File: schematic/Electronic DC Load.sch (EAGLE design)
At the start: 104 parts, among them J1 POWER_JACKPTH_LOCK, J2 AVR_SPI_PROG_3X2PTH, J3 FAN, J4 KF762-2, Q1 16MHz, Q2 IRFP250NV, Q3 600mA/40V, U1 AMS1117-5.0, U10 AD8629ARZ, U2 REF5050_D_8, U3 ATMEGA328P_TQFP, U4 MP1584EN, U5 LM35_LP_3, U6 AD7190BRUZ, U7 AD5541ARZ, U8 INA210AIDCKRG4, U9 PCF8574_DW_16

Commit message: Change debouncing filter network resistor to 1K
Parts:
- R12, R17, R19, R22, R24, R25, R27: value 10K -> 1K
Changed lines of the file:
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@@
 <part name="P+14" library="supply1" library_urn="urn:adsk.eagle:library:371" deviceset="+5V" device=""/>
 <part name="P+15" library="supply1" library_urn="urn:adsk.eagle:library:371" deviceset="+5V" device=""/>
-<part name="R22" library="resistor" library_urn="urn:adsk.eagle:library:348" deviceset="R-EU_" device="R0603" package3d_urn="urn:adsk.eagle:package:26057/1" value="10K"/>
-<part name="R24" library="resistor" library_urn="urn:adsk.eagle:library:348" deviceset="R-EU_" device="R0603" package3d_urn="urn:adsk.eagle:package:26057/1" value="10K"/>
+<part name="R22" library="resistor" library_urn="urn:adsk.eagle:library:348" deviceset="R-EU_" device="R0603" package3d_urn="urn:adsk.eagle:package:26057/1" value="1K"/>
+<part name="R24" library="resistor" library_urn="urn:adsk.eagle:library:348" deviceset="R-EU_" device="R0603" package3d_urn="urn:adsk.eagle:package:26057/1" value="1K"/>
 <part name="GND18" library="supply1" library_urn="urn:adsk.eagle:library:371" deviceset="GND" device=""/>
 <part name="R16" library="resistor" library_urn="urn:adsk.eagle:library:348" deviceset="R-EU_" device="R0603" package3d_urn="urn:adsk.eagle:package:26057/1" value="10K"/>
 <part name="C20" library="resistor" library_urn="urn:adsk.eagle:library:348" deviceset="C-EU" device="C0603" package3d_urn="urn:adsk.eagle:package:26138/1" value="100nF"/>
 <part name="P+8" library="supply1" library_urn="urn:adsk.eagle:library:371" deviceset="+5V" device=""/>
-<part name="R12" library="resistor" library_urn="urn:adsk.eagle:library:348" deviceset="R-EU_" device="R0603" package3d_urn="urn:adsk.eagle:package:26057/1" value="10K"/>
+<part name="R12" library="resistor" library_urn="urn:adsk.eagle:library:348" deviceset="R-EU_" device="R0603" package3d_urn="urn:adsk.eagle:package:26057/1" value="1K"/>
 <part name="C25" library="resistor" library_urn="urn:adsk.eagle:library:348" deviceset="C-EU" device="C0603" package3d_urn="urn:adsk.eagle:package:26138/1" value="100nF"/>
 <part name="C28" library="resistor" library_urn="urn:adsk.eagle:library:348" deviceset="C-EU" device="C0603" package3d_urn="urn:adsk.eagle:package:26138/1" value="100nF"/>
@@
 <part name="P+13" library="supply1" library_urn="urn:adsk.eagle:library:371" deviceset="+5V" device=""/>
 <part name="R20" library="resistor" library_urn="urn:adsk.eagle:library:348" deviceset="R-EU_" device="R0603" package3d_urn="urn:adsk.eagle:package:26057/1" value="10K"/>
-<part name="R19" library="resistor" library_urn="urn:adsk.eagle:library:348" deviceset="R-EU_" device="R0603" package3d_urn="urn:adsk.eagle:package:26057/1" value="10K"/>
+<part name="R19" library="resistor" library_urn="urn:adsk.eagle:library:348" deviceset="R-EU_" device="R0603" package3d_urn="urn:adsk.eagle:package:26057/1" value="1K"/>
 <part name="C24" library="resistor" library_urn="urn:adsk.eagle:library:348" deviceset="C-EU" device="C0603" package3d_urn="urn:adsk.eagle:package:26138/1" value="100nF"/>
 <part name="GND22" library="supply1" library_urn="urn:adsk.eagle:library:371" deviceset="GND" device=""/>
@@
 <part name="P+12" library="supply1" library_urn="urn:adsk.eagle:library:371" deviceset="+5V" device=""/>
 <part name="R18" library="resistor" library_urn="urn:adsk.eagle:library:348" deviceset="R-EU_" device="R0603" package3d_urn="urn:adsk.eagle:package:26057/1" value="10K"/>
-<part name="R17" library="resistor" library_urn="urn:adsk.eagle:library:348" deviceset="R-EU_" device="R0603" package3d_urn="urn:adsk.eagle:package:26057/1" value="10K"/>
+<part name="R17" library="resistor" library_urn="urn:adsk.eagle:library:348" deviceset="R-EU_" device="R0603" package3d_urn="urn:adsk.eagle:package:26057/1" value="1K"/>
 <part name="C23" library="resistor" library_urn="urn:adsk.eagle:library:348" deviceset="C-EU" device="C0603" package3d_urn="urn:adsk.eagle:package:26138/1" value="100nF"/>
 <part name="GND21" library="supply1" library_urn="urn:adsk.eagle:library:371" deviceset="GND" device=""/>
@@
 <part name="P+17" library="supply1" library_urn="urn:adsk.eagle:library:371" deviceset="+5V" device=""/>
 <part name="R28" library="resistor" library_urn="urn:adsk.eagle:library:348" deviceset="R-EU_" device="R0603" package3d_urn="urn:adsk.eagle:package:26057/1" value="10K"/>
-<part name="R27" library="resistor" library_urn="urn:adsk.eagle:library:348" deviceset="R-EU_" device="R0603" package3d_urn="urn:adsk.eagle:package:26057/1" value="10K"/>
+<part name="R27" library="resistor" library_urn="urn:adsk.eagle:library:348" deviceset="R-EU_" device="R0603" package3d_urn="urn:adsk.eagle:package:26057/1" value="1K"/>
 <part name="C27" library="resistor" library_urn="urn:adsk.eagle:library:348" deviceset="C-EU" device="C0603" package3d_urn="urn:adsk.eagle:package:26138/1" value="100nF"/>
 <part name="GND29" library="supply1" library_urn="urn:adsk.eagle:library:371" deviceset="GND" device=""/>
@@
 <part name="P+16" library="supply1" library_urn="urn:adsk.eagle:library:371" deviceset="+5V" device=""/>
 <part name="R26" library="resistor" library_urn="urn:adsk.eagle:library:348" deviceset="R-EU_" device="R0603" package3d_urn="urn:adsk.eagle:package:26057/1" value="10K"/>
-<part name="R25" library="resistor" library_urn="urn:adsk.eagle:library:348" deviceset="R-EU_" device="R0603" package3d_urn="urn:adsk.eagle:package:26057/1" value="10K"/>
+<part name="R25" library="resistor" library_urn="urn:adsk.eagle:library:348" deviceset="R-EU_" device="R0603" package3d_urn="urn:adsk.eagle:package:26057/1" value="1K"/>
 <part name="C26" library="resistor" library_urn="urn:adsk.eagle:library:348" deviceset="C-EU" device="C0603" package3d_urn="urn:adsk.eagle:package:26138/1" value="100nF"/>
 <part name="GND28" library="supply1" library_urn="urn:adsk.eagle:library:371" deviceset="GND" device=""/>

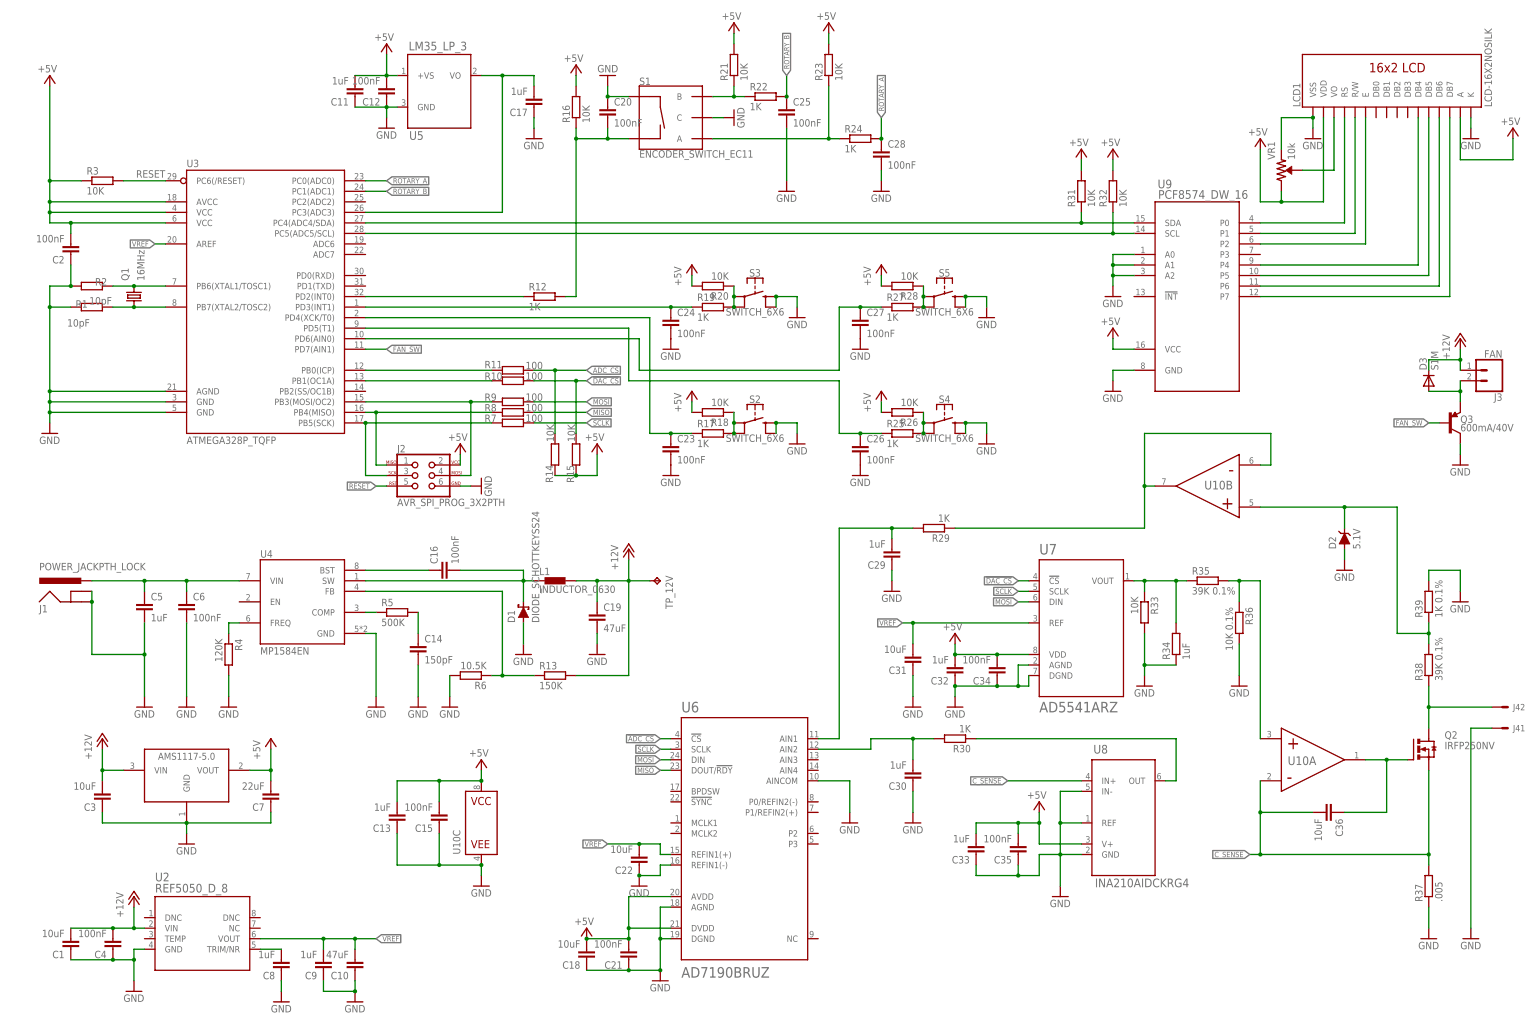
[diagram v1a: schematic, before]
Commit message: Fix lableling errors
Fix a few errors in the labeling of resistors and capacitors
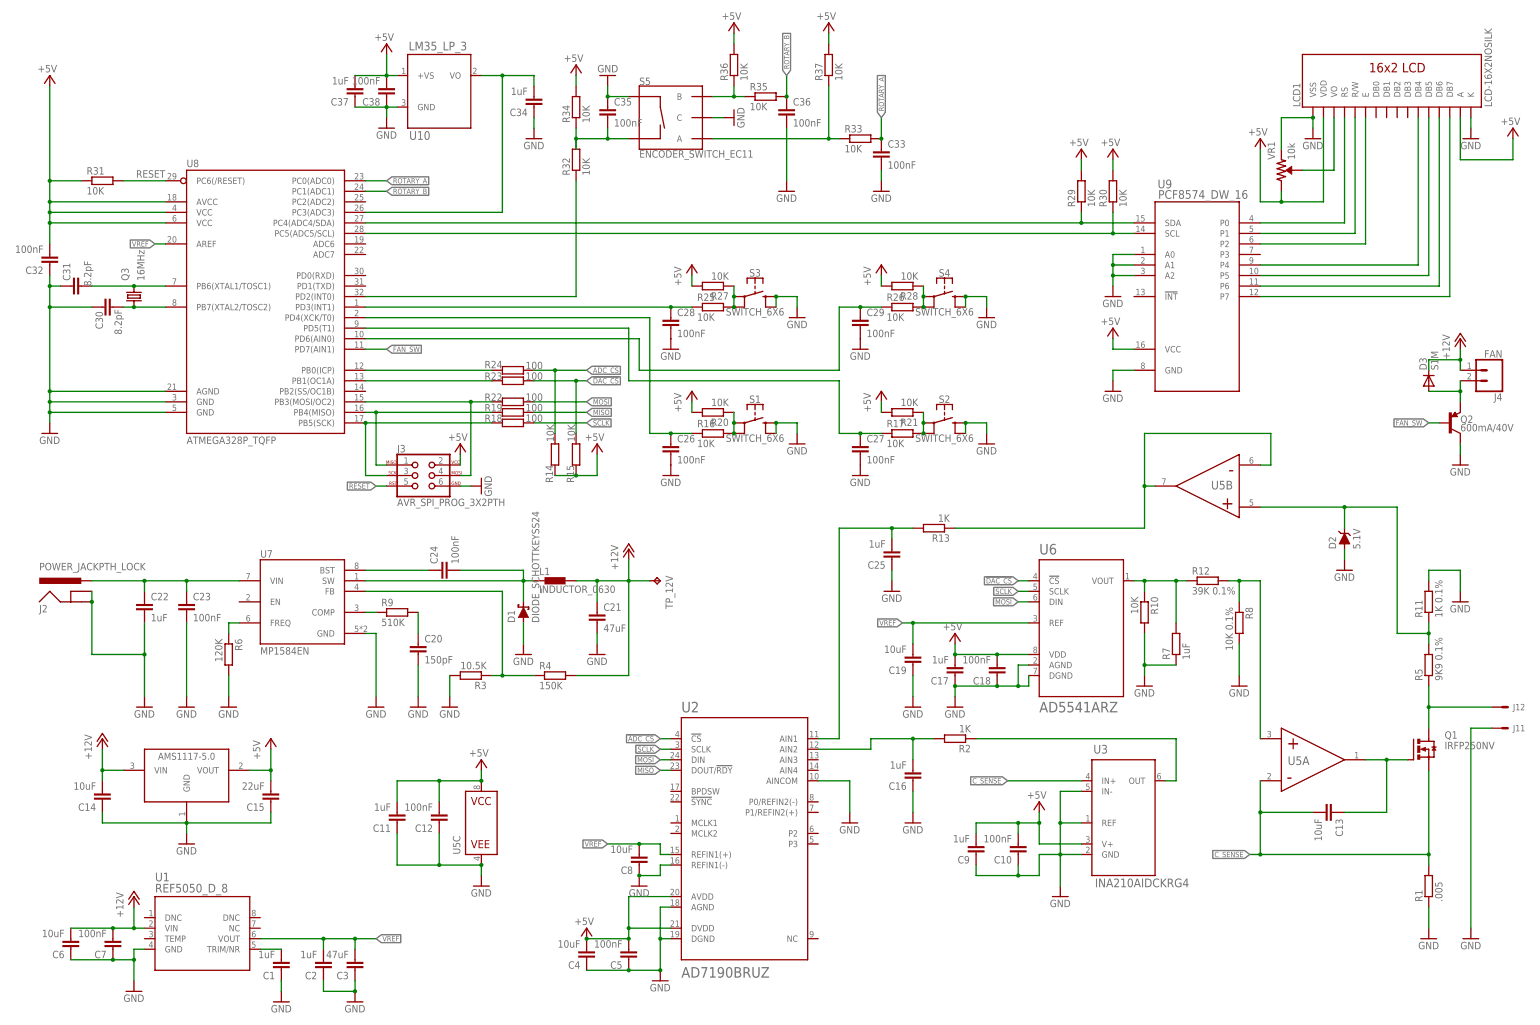
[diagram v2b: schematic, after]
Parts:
- removed R38: 39K 0.1%, resistor:R-EU_M0805
- removed R39: 1K 0.1%, resistor:R-EU_M0805
- added C37: 1uF, resistor:C-EUC0805
- added C38: 100nF, resistor:C-EUC0805
- C1, C22: value 10uF -> 1uF; device resistor:C-EUC1206 -> resistor:C-EUC0805
- C10: value 47uF -> 100nF; device resistor:C-EUC1206 -> resistor:C-EUC0805
- C13, C8: value 1uF -> 10uF; device resistor:C-EUC0805 -> resistor:C-EUC1206
- C14: value 150pF -> 10uF; device resistor:C-EUC0402 -> resistor:C-EUC1206
- C15: value 100nF -> 22uF; device resistor:C-EUC0805 -> resistor:C-EUC1206
- C16, C34: value 100nF -> 1uF
- C18: value 10uF -> 100nF; device resistor:C-EUC1206 -> resistor:C-EUC0805
- C19: value 47uF -> 10uF
- C2, C25: value 100nF -> 1uF; device resistor:C-EUC0603 -> resistor:C-EUC0805
- C20: value 100nF -> 150pF; device resistor:C-EUC0603 -> resistor:C-EUC0402
- C21: value 100nF -> 47uF; device resistor:C-EUC0805 -> resistor:C-EUC1206
- C23, C24: device resistor:C-EUC0603 -> resistor:C-EUC0805
- C29, C32, C33: value 1uF -> 100nF; device resistor:C-EUC0805 -> resistor:C-EUC0603
- C3: value 10uF -> 47uF
- C30: value 1uF -> 8.2pF; device resistor:C-EUC0805 -> resistor:C-EUC0603
- C31: value 10uF -> 8.2pF; device resistor:C-EUC1206 -> resistor:C-EUC0603
- C35: device resistor:C-EUC0805 -> resistor:C-EUC0603
- C36: value 10uF -> 100nF; device resistor:C-EUC1206 -> resistor:C-EUC0603
- C4, C6: value 100nF -> 10uF; device resistor:C-EUC0805 -> resistor:C-EUC1206
- C5: value 1uF -> 100nF
- C7: value 22uF -> 100nF; device resistor:C-EUC1206 -> resistor:C-EUC0805
- J1: value POWER_JACKPTH_LOCK -> KF762-2; device SparkFun-Connectors:POWER_JACKPTH_LOCK -> 0_discrete:KF762-2
- J2: value AVR_SPI_PROG_3X2PTH -> POWER_JACKPTH_LOCK; device SparkFun-Connectors:AVR_SPI_PROG_3X2PTH -> SparkFun-Connectors:POWER_JACKPTH_LOCK
- J3: value FAN -> AVR_SPI_PROG_3X2PTH; device SparkFun-Connectors:CONN_02LOCK_LONGPADS -> SparkFun-Connectors:AVR_SPI_PROG_3X2PTH
- J4: value KF762-2 -> FAN; device 0_discrete:KF762-2 -> SparkFun-Connectors:CONN_02LOCK_LONGPADS
- Q1: value 16MHz -> IRFP250NV; device crystal-geyer_V1_0:KX-7 -> 0_discrete:IRFP250NV
- Q2: value IRFP250NV -> 600mA/40V; device 0_discrete:IRFP250NV -> SparkFun-DiscreteSemi:TRANS_PNP-MMBT4403
- Q3: value 600mA/40V -> 16MHz; device SparkFun-DiscreteSemi:TRANS_PNP-MMBT4403 -> crystal-geyer_V1_0:KX-7
- R1: value 10pF -> .005; device resistor:R-EU_R0805 -> 0_sup:MRE_R005_4W_2728_1%
- R10: value 100 -> 10K; device resistor:R-EU_M0805 -> resistor:R-EU_R0603
- R11: value 100 -> 1K 0.1%
- R12: value 1K -> 39K 0.1%; device resistor:R-EU_R0603 -> resistor:R-EU_R0805
- R13: value 150K -> 1K; device resistor:R-EU_R0603 -> resistor:R-EU_R0805
- R17, R25, R27: value 1K -> 10K
- R18, R23: value 10K -> 100; device resistor:R-EU_R0603 -> resistor:R-EU_M0805
- R19, R22, R24: value 1K -> 100; device resistor:R-EU_R0603 -> resistor:R-EU_M0805
- R2: value 10pF -> 1K
- R29, R30: value 1K -> 10K; device resistor:R-EU_R0805 -> resistor:R-EU_R0603
- R3: value 10K -> 10.5K
- R34: value 1uF -> 10K; device resistor:R-EU_R0805 -> resistor:R-EU_R0603
- R35: value 39K 0.1% -> 10K; device resistor:R-EU_R0805 -> resistor:R-EU_R0603
- R36: value 10K 0.1% -> 10K; device resistor:R-EU_R0805 -> resistor:R-EU_R0603
- R37: value .005 -> 10K; device 0_sup:MRE_R005_4W_2728_1% -> resistor:R-EU_R0603
- R4: value 120K -> 150K
- R5: value 500K -> 9K9 0.1%; device resistor:R-EU_R0603 -> resistor:R-EU_M0805
- R6: value 10.5K -> 120K
- R7: value 100 -> 1uF; device resistor:R-EU_M0805 -> resistor:R-EU_R0805
- R8: value 100 -> 10K 0.1%; device resistor:R-EU_M0805 -> resistor:R-EU_R0805
- R9: value 100 -> 510K; device resistor:R-EU_M0805 -> resistor:R-EU_R0603
- S1: value ENCODER_SWITCH_EC11 -> SWITCH_6X6; device 0_discrete:ENCODER_SWITCH_EC11 -> 0_discrete:SWITCH_6X6
- S5: value SWITCH_6X6 -> ENCODER_SWITCH_EC11; device 0_discrete:SWITCH_6X6 -> 0_discrete:ENCODER_SWITCH_EC11
- TP_12V: value TPB2,54 -> TPB1,27; device testpad:TPB2,54 -> testpad:TPB1,27
- U1: value AMS1117-5.0 -> REF5050_D_8; device AMS1117-5.0:AMS1117-5.0 -> 0_texas-instrument:REF5050_D_8
- U10: value AD8629ARZ -> LM35_LP_3; device 0_analog-devices:AD8629ARZ -> 0_texas-instrument:LM35_LP_3
- U2: value REF5050_D_8 -> AD7190BRUZ; device 0_texas-instrument:REF5050_D_8 -> 0_analog-devices:AD7190BRUZ
- U3: value ATMEGA328P_TQFP -> INA210AIDCKRG4; device SparkFun-IC-Microcontroller:ATMEGA328P_TQFP -> 0_texas-instrument:INA210AIDCKRG4
- U4: value MP1584EN -> AMS1117-5.0; device MP1584EN:MP1584EN -> AMS1117-5.0:AMS1117-5.0
- U5: value LM35_LP_3 -> AD8629ARZ; device 0_texas-instrument:LM35_LP_3 -> 0_analog-devices:AD8629ARZ
- U6: value AD7190BRUZ -> AD5541ARZ; device 0_analog-devices:AD7190BRUZ -> 0_analog-devices:AD5541ARZ
- U7: value AD5541ARZ -> MP1584EN; device 0_analog-devices:AD5541ARZ -> MP1584EN:MP1584EN
- U8: value INA210AIDCKRG4 -> ATMEGA328P_TQFP; device 0_texas-instrument:INA210AIDCKRG4 -> SparkFun-IC-Microcontroller:ATMEGA328P_TQFP
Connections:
- net !ADC_CS: now also R24.2, U2.!CS; no longer R11.2, U6.!CS
- net !DAC_CS: now also R23.2, U6.!CS; no longer R10.2, U7.!CS
- net +12V: now also C14.2, C21.1, C6.2, C7.2, J4.1, R4.2, U4.VIN; no longer C1.2, C19.1, C3.2, C4.2, J3.1, R13.2, U2.VIN
- net +5V: now also C10.2, C17.2, C37.2, C38.2, C4.2, C5.2, C9.2, J3.2, R27.2, R29.2, R30.2, R31.1, R34.2, R36.2, R37.2, U10.+VS, U2.AVDD, U2.DVDD, U3.V+, U4.VOUT, U5C.VCC, U6.VDD, U8.AVCC, U8.VCC@4, U8.VCC@6; no longer C13.2, C2.2, C21.2, C33.2, C34.2, C35.2, C7.2, J2.2, R16.2, R18.2, R23.2, R26.2, R3.1, R31.2, R32.2, U1.VOUT, U10C.VCC, U3.AVCC, U3.VCC@4, U3.VCC@6, U5.+VS, U6.AVDD, U6.DVDD, U7.VDD, U8.V+
- net C_SENSE: now also C13.2, Q1.S, R1.2, U3.IN+, U5A.IN-; no longer C36.2, Q2.S, R37.2, U10A.IN-, U8.IN+
- net FAN_SW: now also Q2.B, U8.PD7(AIN1); no longer Q3.B, U3.PD7(AIN1)
- net GND: now also C14.1, C16.1, C19.1, C20.2, C21.2, C22.2, C25.1, C29.2, C33.2, C36.2, C37.1, C38.1, C5.1, C6.1, J11.S, J2.GND, J2.GNDBREAK, J3.6, Q2.C, R10.2, R11.2, R3.2, R7.1, R8.2, S1.3, S1.4, S5.C, S5.SW+, U10.GND, U2.AGND, U2.AINCOM, U2.DGND, U2.REFIN1(-), U3.GND, U3.IN-, U3.REF, U5C.VEE, U7.GND, U8.AGND, U8.GND@3, U8.GND@5; no longer C13.1, C14.2, C19.2, C20.1, C21.1, C22.1, C24.2, C25.2, C29.1, C33.1, C5.2, C6.2, J1.GND, J1.GNDBREAK, J2.6, J41.S, Q3.C, R2.1, R33.2, R34.1, R36.2, R37.1, R39.2, R4.2, S1.C, S1.SW+, S5.3, S5.4, U10C.VEE, U2.GND, U3.AGND, U3.GND@3, U3.GND@5, U5.GND, U6.AINCOM, U6.REFIN1(-), U7.AGND, U7.DGND, U8.GND, U8.IN-, U8.REF
- net MISO: now also R19.2, U2.DOUT/!RDY; no longer R8.2, U6.DOUT/!RDY
- net MOSI: now also R22.2, U2.DIN; no longer R9.2, U7.DIN
- net N$1: now also R29.1, U8.PC4(ADC4/SDA); no longer R31.1, U3.PC4(ADC4/SDA)
- net N$10: now also C1.2, U1.TRIM/NR; no longer C8.2, U2.TRIM/NR
- net N$11: now also C31.2, Q3.2, U8.PB6(XTAL1/TOSC1); no longer Q1.2, R2.2, U3.PB6(XTAL1/TOSC1)
- net N$12: now also C30.2, Q3.1, U8.PB7(XTAL2/TOSC2); no longer Q1.1, R1.2, U3.PB7(XTAL2/TOSC2)
- net N$14: now also J12.S, Q1.D, R5.1; no longer J42.S, Q2.D, R38.1
- net N$15: now also C34.2, U10.VO, U8.PC3(ADC3); no longer C17.2, U3.PC3(ADC3), U5.VO
- net N$16: now also C25.2, R13.2, U2.AIN1; no longer C29.2, R29.2, U6.AIN1
- net N$17: now also R6.1, U7.FREQ; no longer R4.1, U4.FREQ
- net N$18: now also R2.1, U3.OUT; no longer R30.1, U8.OUT
- net N$19: now also C24.1, U7.BST; no longer C16.1, U4.BST
- net N$2: now also R30.1, U8.PC5(ADC5/SCL); no longer R32.1, U3.PC5(ADC5/SCL)
- net N$20: now also C22.1, C23.1, J2.PWR, U7.VIN; no longer C5.1, C6.1, J1.PWR, U4.VIN
- net N$21: now also C24.2, U7.SW; no longer C16.2, U4.SW
- net N$22: now also R3.1, R4.1, U7.FB; no longer R13.1, R6.1, U4.FB
- net N$23: now also R9.1, U7.COMP; no longer R5.1, U4.COMP
- net N$24: now also C16.2, R2.2, U2.AIN2; no longer C30.2, R30.2, U6.AIN2
- net N$25: now also C20.1, R9.2; no longer C14.1, R5.2
- net N$26: now also R10.1, R12.1, R7.2, U6.VOUT; no longer R33.1, R34.2, R35.1, U7.VOUT
- net N$27: now also R13.1, U5B.IN-, U5B.OUT; no longer R29.1, U10B.IN-, U10B.OUT
- net N$28: now also J4.2, Q2.E; no longer J3.2, Q3.E
- net N$29: now also R35.1, R36.1, S5.B; no longer R21.1, R22.1, S1.B
- net N$30: now also J3.3, R18.1, U8.PB5(SCK); no longer J2.3, R7.1, U3.PB5(SCK)
- net N$31: now also J3.1, R19.1, U8.PB4(MISO); no longer J2.1, R8.1, U3.PB4(MISO)
- net N$32: now also J3.4, R22.1, U8.PB3(MOSI/OC2); no longer J2.4, R9.1, U3.PB3(MOSI/OC2)
- net N$34: now also R23.1, U8.PB1(OC1A); no longer R10.1, U3.PB1(OC1A)
- net N$35: now also R24.1, U8.PB0(ICP); no longer R11.1, U3.PB0(ICP)
- net N$36: now also C13.1, Q1.G, U5A.OUT; no longer C36.1, Q2.G, U10A.OUT
- net N$37: now also R11.1, R5.2, U5B.IN+; no longer R38.2, R39.1, U10B.IN+
- net N$38: now also R33.1, R37.1, S5.A; no longer R23.1, R24.1, S1.A
- net N$39: now also R12.2, R8.1, U5A.IN+; no longer R35.2, R36.1, U10A.IN+
- net N$40: now also R16.2, R20.1, S1.1, S1.2; no longer R17.2, R18.1, S2.1, S2.2
- net N$41: now also R25.2, R27.1; no longer R19.2, R20.1
- net N$42: now also C35.2, R32.2, R34.1, S5.SW-; no longer C20.2, R12.2, R16.1, S1.SW-
- net N$43: now also C26.1, R16.1, U8.PD4(XCK/T0); no longer C23.1, R17.1, U3.PD4(XCK/T0)
- net N$44: now also R32.1, U8.PD2(INT0); no longer R12.1, U3.PD2(INT0)
- net N$46: now also C28.1, R25.1, U8.PD3(INT1); no longer C24.1, R19.1, U3.PD3(INT1)
- net N$48: now also R26.2, S4.1, S4.2; no longer R27.2, S5.1, S5.2
- net N$51: now also R17.2, R21.1, S2.1, S2.2; no longer R25.2, R26.1, S4.1, S4.2
- net N$52: now also C27.1, R17.1, U8.PD5(T1); no longer C26.1, R25.1, U3.PD5(T1)
- net N$55: now also C29.1, R26.1, U8.PD6(AIN0); no longer C27.1, R27.1, U3.PD6(AIN0)
- net RESET: now also J3.5, R31.2, U8.PC6(/RESET); no longer J2.5, R3.2, U3.PC6(/RESET)
- net ROTARY_A: now also C33.1, R33.2, U8.PC0(ADC0); no longer C28.1, R24.2, U3.PC0(ADC0)
- net ROTARY_B: now also C36.1, R35.2, U8.PC1(ADC1); no longer C25.1, R22.2, U3.PC1(ADC1)
- net SCLK: now also R18.2, U2.SCLK; no longer R7.2, U7.SCLK
- net VREF: now also C19.2, C2.2, C3.2, C8.2, U1.VOUT, U2.REFIN1(+), U6.REF, U8.AREF; no longer C10.2, C22.2, C31.2, C9.2, U2.VOUT, U3.AREF, U6.REFIN1(+), U7.REF
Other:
- moved on the sheet: C1, C10, C11, C12, C13, C14, C15, C16, C17, C18, C19, C2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

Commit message: Remove the ground bridge for Rsense
I made the ground bridge not sure if it's needed.
And obviously, it doesn't. And removing it will tremendously increase the accuracy of INA213!!!
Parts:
- removed R10: 10K, resistor:R-EU_R0603
- D2: device 0_discrete:DIODE-ZENER-5.1V -> 0_discrete:DIODE-ZENER-ZMM5.1
- R7: device resistor:R-EU_R0805 -> resistor:C-EUC0805
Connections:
- net GND: no longer R10.2
- net N$26: no longer R10.1
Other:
- moved on the sheet: R7
